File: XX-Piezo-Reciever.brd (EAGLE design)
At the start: 30.7 x 26.2 mm, 9 parts, among them IC1 TL072D, J1 AVR_SPI_PROG_3X2PTH, U1 ATMEGA1284P-AU

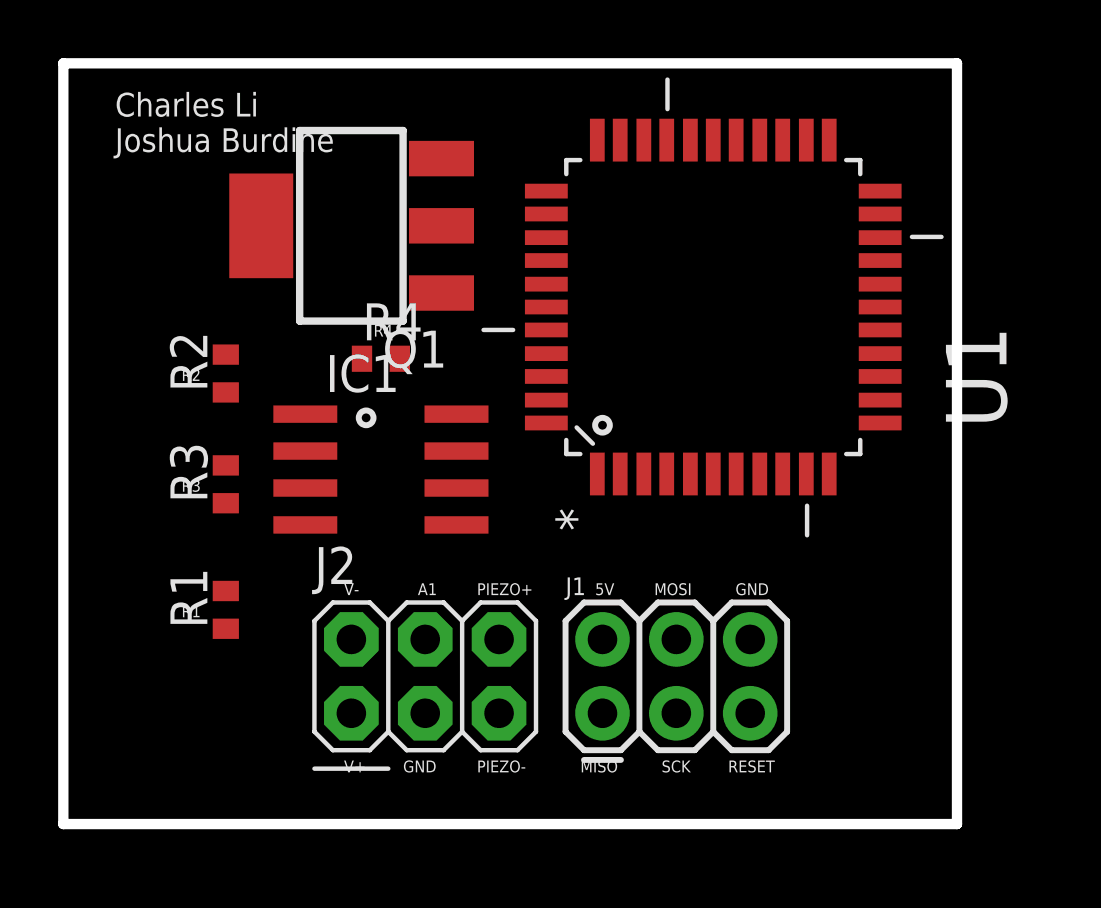
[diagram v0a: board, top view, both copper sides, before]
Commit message: Added correct mosfet, finished routing. No decoup caps yet.
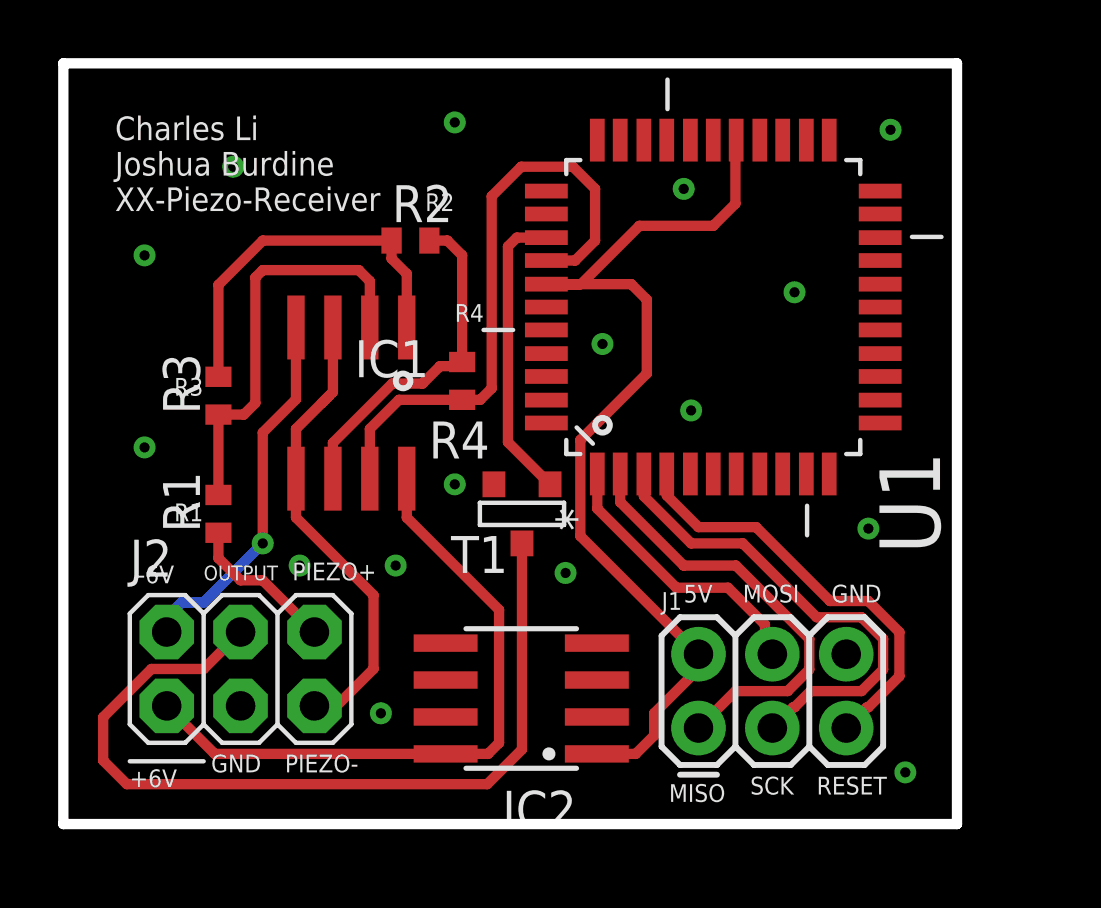
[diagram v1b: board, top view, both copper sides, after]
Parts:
- removed Q1: (no value), m-pad-2.1:SOT223
- added IC2: L78LXXBD/CD, v-reg-3:SO08
- added T1: (no value), zetex:SOT-23
- moved R2 7.82 mm to (11.9, 20.1), turned to 0 degrees
- moved J2 6.36 mm to (6.10, 5.33)
- moved J1 3.34 mm to (21.8, 3.30)
- moved R1 3.31 mm to (5.33, 10.7)
- moved R3 3.06 mm to (5.33, 14.7)
- moved R4 2.90 mm to (13.7, 15.2), turned to 270 degrees
- moved IC1 2.50 mm to (9.91, 14.5), turned to 180 degrees
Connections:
- net +5V: now also IC2.1
- net +6V: now also IC2.8
- net A1: now also T1.3; no longer Q1.1
- net GND: now also IC2.2, T1.2; no longer Q1.3
- net OUTPUT: now also T1.1; no longer Q1.2
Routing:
- net +5V: track 0.00 -> 35.1 mm
- net OUTPUT: track 0.00 -> 29.7 mm
- net +6V: track 0.00 -> 22.7 mm
- net OUT2: track 0.00 -> 21.1 mm
- net SCK: track 0.00 -> 16.7 mm
- net PIEZO-: track 0.00 -> 16.3 mm
- net MISO: track 0.00 -> 15.1 mm
- net RESET: track 0.00 -> 14.8 mm
- net PIEZO+1: track 0.00 -> 14.3 mm
- net OUT1: track 0.00 -> 12.9 mm
- net -6V: track 0.00 -> 12.8 mm, vias 0 -> 1
- net PIEZO+2: track 0.00 -> 11.8 mm
- net A1: track 0.00 -> 10.2 mm
- net MOSI: track 0.00 -> 9.73 mm
- net PIEZO+: track 0.00 -> 5.23 mm
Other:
- board text added: "+6V"
- board text added: "-6V"
- board text added: "Charles Li Joshua Burdine XX-Piezo-Receiver"
- board text added: "OUTPUT"
- board text removed: "A1"
- board text removed: "Charles Li Joshua Burdine"
- board text removed: "V+"
- board text removed: "V-"
